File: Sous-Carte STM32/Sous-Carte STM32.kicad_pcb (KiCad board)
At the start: 2 copper layers, 117.5 x 123 mm, 34 parts, among them J1 RJ45, P1 CONN_25X2, P2 CONN_25X2, P3 CONN_4, P5 CONN_25X2, P6 CONN_2, P7 CONN_2, P8 CONN_2

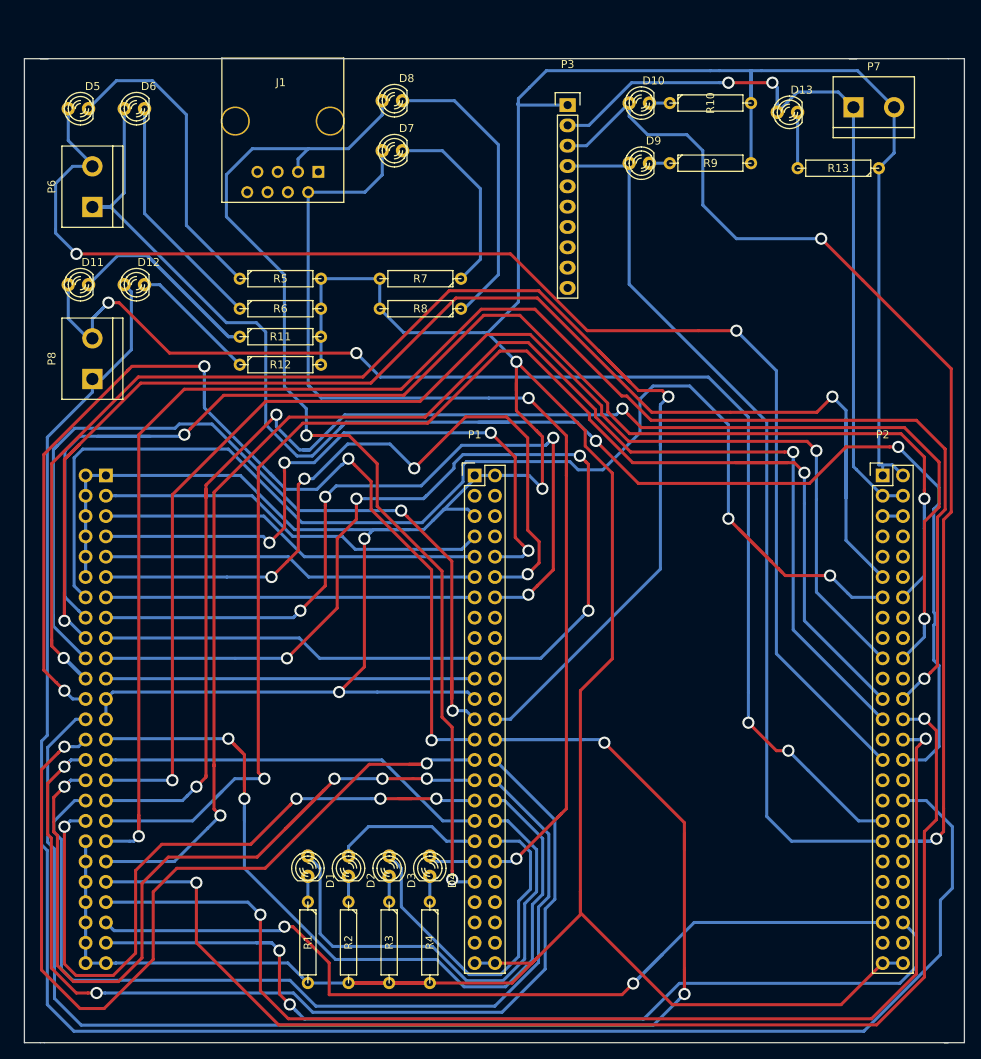
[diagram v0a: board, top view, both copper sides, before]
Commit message: ajout texte et plan de masse
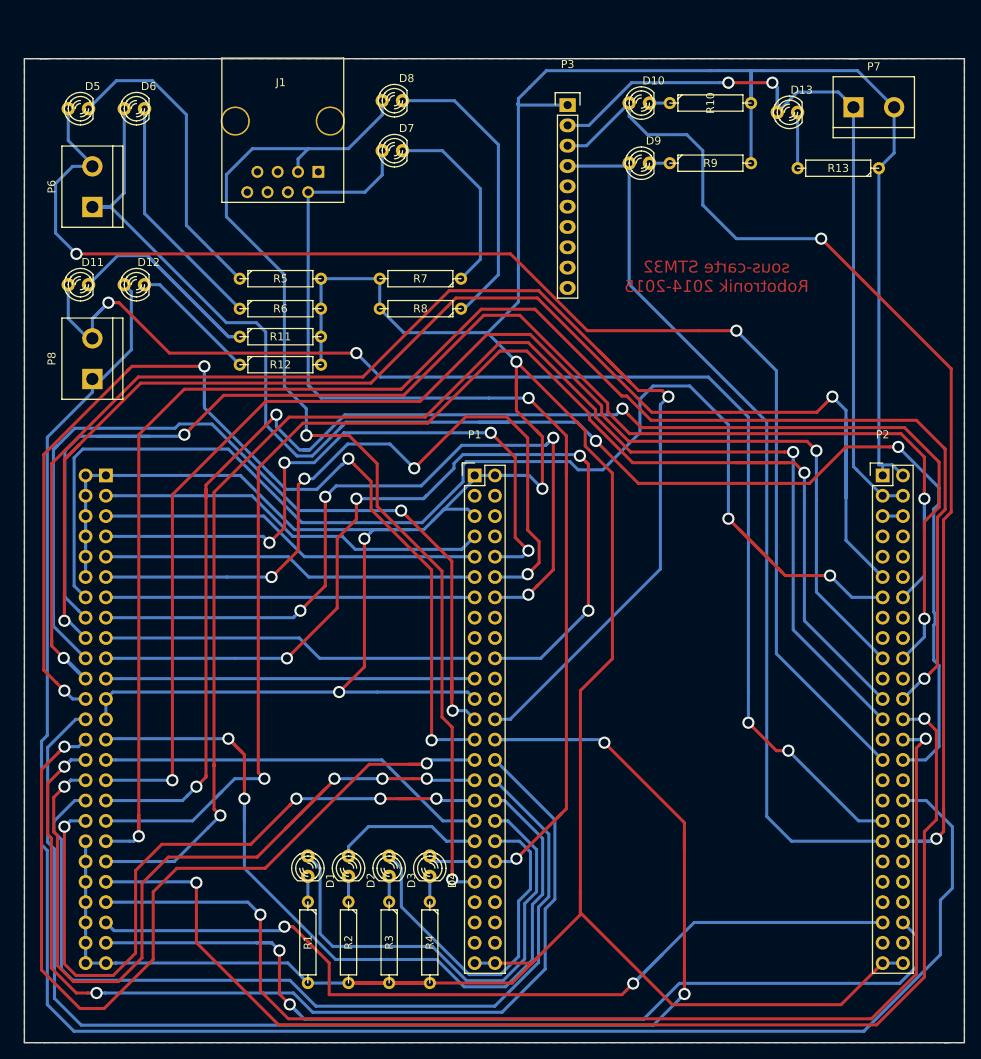
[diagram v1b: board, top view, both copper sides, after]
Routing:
- added copper zone on B.Cu, net GND
- added copper zone on F.Cu, net GND
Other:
- board text added: "sous-carte STM32 Robotronik 2014-2015"
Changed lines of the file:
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@@
   (general
     (links 112)
-    (no_connects 2)
+    (no_connects 0)
     (area 87.449999 45.394 205.050001 169.050001)
     (thickness 1.6)
-    (drawings 11)
+    (drawings 12)
     (tracks 1030)
     (zones 0)
@@
       (rotate (xyz 0 0 90))
     )
+  )
+  (gr_text "sous-carte STM32\nRobotronik 2014-2015" (at 174 73.25) (layer F.Cu)
+    (effects (font (size 1.5 1.5) (thickness 0.3)) (justify mirror))
   )
   (gr_line (start 87.5 46) (end 89.5 46) (layer Edge.Cuts) (width 0.1))
@@
   (segment (start 97.21 86.04) (end 100.871501 82.378499) (width 0.381) (layer B.Cu) (net 108))
   (segment (start 100.871501 75.141501) (end 100.818199 75.088199) (width 0.381) (layer B.Cu) (net 108))
+  (zone (net 7) (net_name GND) (layer F.Cu) (hatch edge 0.508)
+    (connect_pads (clearance 0.508))
+    (min_thickness 0.254)
+    (fill yes (arc_segments 16) (thermal_gap 0.508) (thermal_bridge_width 0.508))
+    (polygon
+      (pts
+        (xy 205 169) (xy 205 46) (xy 87.5 46) (xy 87.5 169)
+      )
+    )
+  )
+  (zone (net 7) (net_name GND) (layer B.Cu) (hatch edge 0.508)
+    (connect_pads (clearance 0.508))
+    (min_thickness 0.254)
+    (fill yes (arc_segments 16) (thermal_gap 0.508) (thermal_bridge_width 0.508))
+    (polygon
+      (pts
+        (xy 205 169) (xy 205 46) (xy 87.5 46) (xy 87.5 169)
+      )
+    )
+  )
 )

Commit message: nettoyage
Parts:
- P3: footprint Pin_Headers:Pin_Header_Straight_1x10 -> Pin_Headers:Pin_Header_Straight_1x04
- moved D2 2.58 mm to (125.5, 147.5)
- moved R2 2.52 mm to (125.5, 156.5)
- moved D1 2.50 mm to (120.5, 147.5)
- moved R1 2.44 mm to (120.5, 156.5)
- moved D3 2.17 mm to (131.0, 147.5)
- moved R3 2.10 mm to (131.0, 156.5)
- moved D4 1.77 mm to (136.5, 147.5)
- moved R4 1.68 mm to (136.5, 156.5)
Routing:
- net B5: track 152.9 -> 170.7 mm
- net GND: track 642.6 -> 630.3 mm
- net UART3_TX: track 133.8 -> 144.3 mm
- net E5: track 174.4 -> 164.7 mm
- net E15: track 88.9 -> 97.5 mm
- net E14: track 113.8 -> 122.0 mm
- net C8: track 112.4 -> 104.6 mm
- net B3: track 150.8 -> 158.3 mm
- net E11: track 108.3 -> 115.7 mm
- net B14: track 44.7 -> 52.0 mm
- net E12: track 126.4 -> 133.2 mm
- net B15: track 5.89 -> 12.5 mm
- net B13: track 18.7 -> 25.1 mm
- net B10: track 104.0 -> 110.1 mm
- net UART4_TX: track 112.4 -> 106.4 mm
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
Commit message: ajout texte
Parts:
- moved R13 3.32 mm to (189.5, 63.0)
- moved D1 3.00 mm to (117.5, 147.5)
- moved D2 3.00 mm to (122.5, 147.5)
- moved D3 3.00 mm to (128.0, 147.5)
- moved D4 3.00 mm to (133.5, 147.5)
- moved R1 3.00 mm to (117.5, 156.5)
- moved R2 3.00 mm to (122.5, 156.5)
- moved R3 3.00 mm to (128.0, 156.5)
- moved R4 3.00 mm to (133.5, 156.5)
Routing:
- net E6: track 174.7 -> 164.7 mm
- net E9: track 140.4 -> 130.6 mm
- net B13: track 25.1 -> 31.5 mm
- net Net-(D13-Pad2): track 6.98 -> 10.4 mm
- net D9: track 136.9 -> 139.9 mm
- net B12: track 64.9 -> 68.0 mm
- net B15: track 12.5 -> 15.5 mm
- net B9: track 185.9 -> 188.8 mm
- net UART2_TX: track 170.9 -> 168.1 mm
- net B10: track 110.1 -> 112.3 mm
- net B4: track 185.0 -> 186.9 mm
- net B14: track 52.0 -> 53.2 mm
- net UART2_RX: track 198.6 -> 199.6 mm
- net UART4_RX: track 134.4 -> 135.3 mm
- net E5: track 164.7 -> 164.1 mm
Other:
- board text added: "1"
- board text added: "2"
- board text added: "3"
- board text added: "4"
- board text added: "5V"
- board text added: "Asser"
- board text added: "GND"
- board text added: "PWR"
- board text added: "RX"
- board text added: "TX"
- board text added: "Xbee"
- board text added: "zone STM32"

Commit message: DRC ok
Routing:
- net UART2_TX: track 168.1 -> 167.2 mm
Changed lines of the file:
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@@
     (thickness 1.6)
     (drawings 53)
-    (tracks 996)
+    (tracks 997)
     (zones 0)
     (modules 34)
@@
   (segment (start 160.62 56.88) (end 155.4 56.88) (width 0.381) (layer B.Cu) (net 8))
   (segment (start 163.095 54.405) (end 160.62 56.88) (width 0.381) (layer B.Cu) (net 8))
-  (segment (start 153.022499 69) (end 150.624127 69) (width 0.381) (layer F.Cu) (net 9))
+  (segment (start 148.356332 68.5) (end 96.57763 68.5) (width 0.381) (layer F.Cu) (net 9))
+  (segment (start 150.124127 68.5) (end 148.356332 68.5) (width 0.381) (layer F.Cu) (net 9))
+  (segment (start 164.022499 80) (end 153.479047 69.456548) (width 0.381) (layer F.Cu) (net 9))
+  (segment (start 152.522499 68.5) (end 153.479047 69.456548) (width 0.381) (layer F.Cu) (net 9))
+  (segment (start 148.356332 68.5) (end 152.522499 68.5) (width 0.381) (layer F.Cu) (net 9))
+  (segment (start 94.738001 67.738001) (end 95.5 68.5) (width 0.381) (layer B.Cu) (net 9))
+  (segment (start 93.5 61.96) (end 93.5 66.5) (width 0.381) (layer B.Cu) (net 9))
+  (segment (start 96.57763 68.5) (end 95.5 68.5) (width 0.381) (layer F.Cu) (net 9))
+  (segment (start 96 59.46) (end 93.5 61.96) (width 0.381) (layer B.Cu) (net 9))
+  (segment (start 93.5 66.5) (end 94.738001 67.738001) (width 0.381) (layer B.Cu) (net 9))
+  (via (at 95.5 68.5) (size 1.524) (drill 1) (layers F.Cu B.Cu) (net 9))
   (segment (start 175.000002 80) (end 164.022499 80) (width 0.381) (layer F.Cu) (net 9))
-  (segment (start 164.022499 80) (end 153.022499 69) (width 0.381) (layer F.Cu) (net 9))
-  (segment (start 150.624127 69) (end 96.57763 69) (width 0.381) (layer F.Cu) (net 9))
-  (segment (start 150.624127 69) (end 153 69) (width 0.381) (layer F.Cu) (net 9))
   (segment (start 180.380469 119.253469) (end 180.380469 85.380467) (width 0.381) (layer B.Cu) (net 9))
   (segment (start 175.762001 80.761999) (end 175.000002 80) (width 0.381) (layer B.Cu) (net 9))
   (segment (start 194.782 133.655) (end 180.380469 119.253469) (width 0.381) (layer B.Cu) (net 9))
-  (segment (start 96.57763 69) (end 95.5 69) (width 0.381) (layer F.Cu) (net 9))
   (segment (start 180.380469 85.380467) (end 175.762001 80.761999) (width 0.381) (layer B.Cu) (net 9))
   (via (at 175.000002 80) (size 1.524) (drill 1) (layers F.Cu B.Cu) (net 9))
-  (segment (start 96 59.46) (end 93.5 61.96) (width 0.381) (layer B.Cu) (net 9))
-  (segment (start 93.5 61.96) (end 93.5 67) (width 0.381) (layer B.Cu) (net 9))
-  (segment (start 93.5 67) (end 94.738001 68.238001) (width 0.381) (layer B.Cu) (net 9))
-  (segment (start 94.738001 68.238001) (end 95.5 69) (width 0.381) (layer B.Cu) (net 9))
-  (via (at 95.5 69) (size 1.524) (drill 1) (layers F.Cu B.Cu) (net 9))
   (segment (start 92.98 56.23) (end 92.98 52.25) (width 0.381) (layer B.Cu) (net 9))
   (segment (start 96 59.25) (end 92.98 56.23) (width 0.381) (layer B.Cu) (net 9))

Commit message: bougé la carte
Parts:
- moved D1 5.10 mm to (116.5, 142.5)
- moved D10 5.10 mm to (163.4, 46.5)
- moved D11 5.10 mm to (93.2, 69.2)
- moved D12 5.10 mm to (100.2, 69.2)
- moved D13 5.10 mm to (181.9, 47.7)
- moved D2 5.10 mm to (121.5, 142.5)
- moved D3 5.10 mm to (127.0, 142.5)
- moved D4 5.10 mm to (132.5, 142.5)
- moved D5 5.10 mm to (93.2, 47.2)
- moved D6 5.10 mm to (100.2, 47.2)
- moved D7 5.10 mm to (132.5, 52.5)
- moved D8 5.10 mm to (132.5, 46.2)
- moved D9 5.10 mm to (163.4, 54.1)
- moved J1 5.10 mm to (118.8, 48.8)
- moved P1 5.10 mm to (142.8, 93.1)
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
